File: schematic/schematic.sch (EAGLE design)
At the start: 4 parts

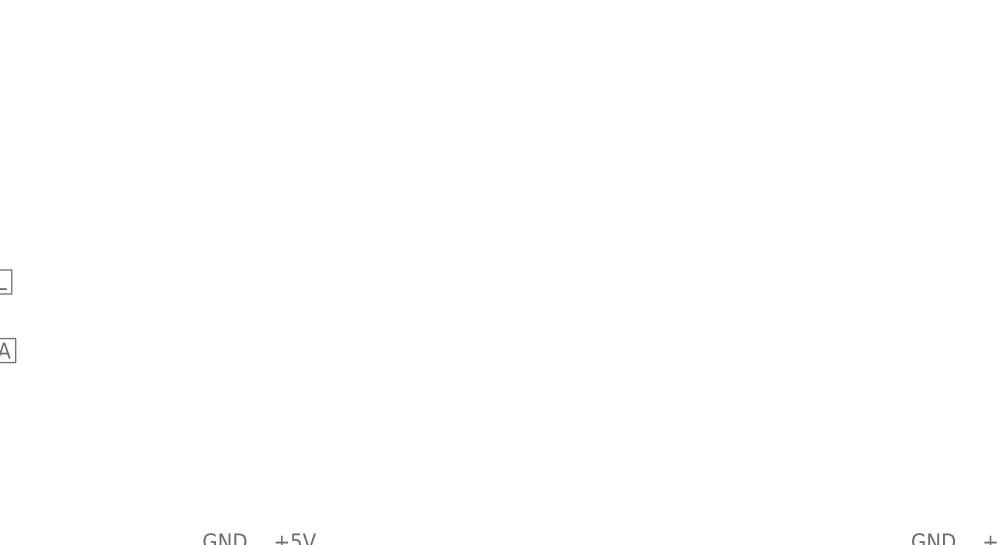
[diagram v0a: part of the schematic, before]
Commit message: Update schematic for radio module. Add eagle lib
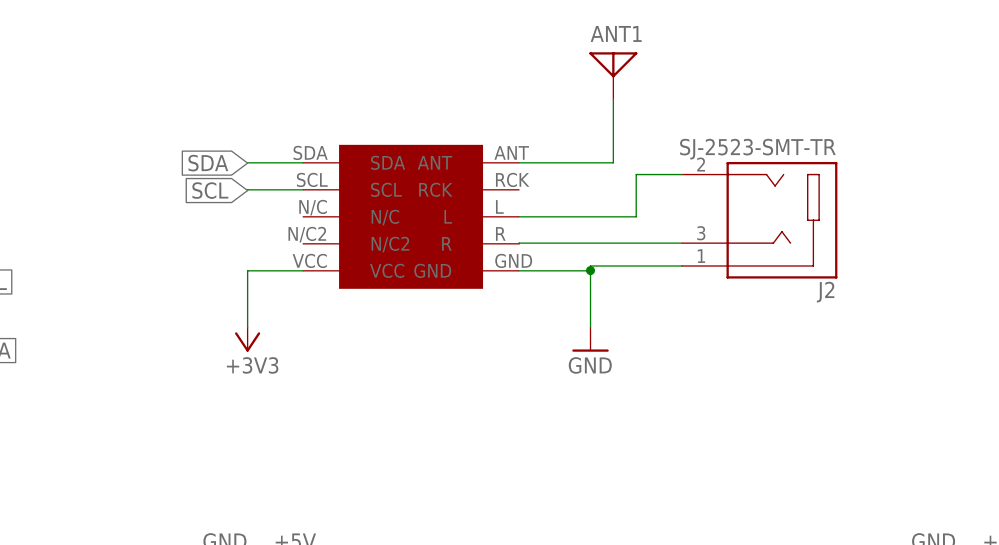
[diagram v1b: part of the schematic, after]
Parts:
- added ANT1: (no value), discrete:ANTENNA
- added J2: SJ-2523-SMT-TR, Audio Connectors:SJ-2523-SMT-TR
- added U$1: RDA, RDA:RDA
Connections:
- new net +3V3: U$1.VCC
- new net N$1: ANT1.1, U$1.ANT
- new net N$2: J2.TIP, U$1.L
- new net N$3: J2.RING, U$1.R
- net GND: now also J2.SLEEVE, U$1.GND
- net SCL: now also U$1.SCL
- net SDA: now also U$1.SDA
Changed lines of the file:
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@@
 <schematic_group name="USER_CONTROLLER"/>
 <schematic_group name="AUDIO_CONTOLLER"/>
+<schematic_group name="RADIO_MODULE"/>
 </groups>
 <parts>
@@
 <part name="R2" library="rcl" library_urn="urn:adsk.eagle:library:334" deviceset="R-EU_" device="0204/7" package3d_urn="urn:adsk.eagle:package:23498/2" value="4.7k"/>
 <part name="P+1" library="supply1" library_urn="urn:adsk.eagle:library:371" deviceset="+5V" device=""/>
+<part name="U$1" library="RDA" deviceset="RDA" device=""/>
+<part name="GND3" library="supply1" library_urn="urn:adsk.eagle:library:371" deviceset="GND" device=""/>
+<part name="ANT1" library="discrete" library_urn="urn:adsk.eagle:library:211" deviceset="ANTENNA" device="" package3d_urn="urn:adsk.eagle:package:12928/1"/>
+<part name="J2" library="Audio Connectors" library_urn="urn:adsk.eagle:library:16251796" deviceset="SJ-2523-SMT-TR" device="" package3d_urn="urn:adsk.eagle:package:16225688/4"/>
+<part name="+3V1" library="supply1" library_urn="urn:adsk.eagle:library:371" deviceset="+3V3" device=""/>
 </parts>
 <sheets>
@@
 <attribute name="VALUE" x="2.54" y="121.92" size="1.778" layer="96" rot="R180"/>
 </instance>
+<instance part="U$1" gate="G$1" x="63.5" y="124.46" smashed="yes" grouprefs="RADIO_MODULE"/>
+<instance part="GND3" gate="1" x="91.44" y="101.6" smashed="yes" grouprefs="RADIO_MODULE">
+<attribute name="VALUE" x="88.9" y="99.06" size="1.778" layer="96"/>
+</instance>
+<instance part="ANT1" gate="A" x="93.98" y="134.62" smashed="yes" grouprefs="RADIO_MODULE">
+<attribute name="NAME" x="91.44" y="135.89" size="1.778" layer="95"/>
+<attribute name="VALUE" x="96.52" y="129.54" size="1.778" layer="96"/>
+</instance>
+<instance part="J2" gate="G$1" x="114.3" y="116.078" smashed="yes" rot="R180" grouprefs="RADIO_MODULE">
+<attribute name="NAME" x="118.74991875" y="109.21475" size="1.77915" layer="95" rot="R180"/>
+<attribute name="VALUE" x="118.74648125" y="125.09688125" size="1.77835" layer="96" rot="R180"/>
+</instance>
+<instance part="+3V1" gate="G$1" x="53.34" y="101.6" smashed="yes" rot="R180">
+<attribute name="VALUE" x="50.8" y="99.06" size="1.778" layer="96"/>
+</instance>
 </instances>
 <busses>
@@
 <label x="20.32" y="109.22" size="1.778" layer="95" xref="yes" grouprefs="I2C"/>
 </segment>
+<segment>
+<pinref part="U$1" gate="G$1" pin="SCL"/>
+<wire x1="59.5" y1="119.46" x2="53.34" y2="119.46" width="0.1524" layer="91" grouprefs="RADIO_MODULE"/>
+<wire x1="53.34" y1="119.46" x2="53.34" y2="119.38" width="0.1524" layer="91" grouprefs="RADIO_MODULE"/>
+<label x="53.34" y="119.38" size="1.778" layer="95" rot="R180" xref="yes" grouprefs="RADIO_MODULE"/>
+</segment>
 </net>
 <net name="SDA" class="0">
@@
 <wire x1="15.24" y1="101.6" x2="20.32" y2="101.6" width="0.1524" layer="91" grouprefs="I2C"/>
 <label x="20.32" y="101.6" size="1.778" layer="95" xref="yes" grouprefs="I2C"/>
+</segment>
+<segment>
+<pinref part="U$1" gate="G$1" pin="SDA"/>
+<wire x1="59.5" y1="122.46" x2="53.34" y2="122.46" width="0.1524" layer="91" grouprefs="RADIO_MODULE"/>
+<label x="53.34" y="122.428" size="1.778" layer="95" rot="R180" xref="yes" grouprefs="RADIO_MODULE"/>
 </segment>
 </net>
@@
 <wire x1="129.54" y1="76.2" x2="129.54" y2="63.5" width="0.1524" layer="91" grouprefs="AUDIO_CONTOLLER"/>
 <wire x1="129.54" y1="63.5" x2="119.38" y2="63.5" width="0.1524" layer="91" grouprefs="AUDIO_CONTOLLER"/>
+</segment>
+<segment>
+<pinref part="U$1" gate="G$1" pin="GND"/>
+<pinref part="GND3" gate="1" pin="GND"/>
+<wire x1="83.5" y1="110.46" x2="91.44" y2="110.46" width="0.1524" layer="91" grouprefs="RADIO_MODULE"/>
+<pinref part="J2" gate="G$1" pin="SLEEVE"/>
+<wire x1="91.44" y1="110.46" x2="91.44" y2="104.14" width="0.1524" layer="91" grouprefs="RADIO_MODULE"/>
+<wire x1="101.6" y1="110.998" x2="91.44" y2="110.998" width="0.1524" layer="91" grouprefs="RADIO_MODULE"/>
+<wire x1="91.44" y1="110.998" x2="91.44" y2="110.49" width="0.1524" layer="91" grouprefs="RADIO_MODULE"/>
+<junction x="91.44" y="110.49" grouprefs="RADIO_MODULE"/>
+<wire x1="91.44" y1="110.49" x2="91.44" y2="110.46" width="0.1524" layer="91" grouprefs="RADIO_MODULE"/>
 </segment>
 </net>
@@
 </segment>
 </net>
+<net name="N$1" class="0">
+<segment>
+<pinref part="ANT1" gate="A" pin="1"/>
+<wire x1="93.98" y1="129.54" x2="93.98" y2="122.46" width="0.1524" layer="91" grouprefs="RADIO_MODULE"/>
+<pinref part="U$1" gate="G$1" pin="ANT"/>
+<wire x1="93.98" y1="122.46" x2="83.5" y2="122.46" width="0.1524" layer="91" grouprefs="RADIO_MODULE"/>
+</segment>
+</net>
+<net name="N$2" class="0">
+<segment>
+<pinref part="J2" gate="G$1" pin="TIP"/>
+<pinref part="U$1" gate="G$1" pin="L"/>
+<wire x1="101.6" y1="121.158" x2="96.52" y2="121.158" width="0.1524" layer="91" grouprefs="RADIO_MODULE"/>
+<wire x1="96.52" y1="121.158" x2="96.52" y2="116.46" width="0.1524" layer="91" grouprefs="RADIO_MODULE"/>
+<wire x1="96.52" y1="116.46" x2="83.5" y2="116.46" width="0.1524" layer="91" grouprefs="RADIO_MODULE"/>
+</segment>
+</net>
+<net name="N$3" class="0">
+<segment>
+<pinref part="J2" gate="G$1" pin="RING"/>
+<pinref part="U$1" gate="G$1" pin="R"/>
+<wire x1="101.6" y1="113.538" x2="83.5" y2="113.538" width="0.1524" layer="91" grouprefs="RADIO_MODULE"/>
+<wire x1="83.5" y1="113.538" x2="83.5" y2="113.46" width="0.1524" layer="91" grouprefs="RADIO_MODULE"/>
+</segment>
+</net>
+<net name="+3V3" class="0">
+<segment>
+<wire x1="53.34" y1="104.14" x2="53.34" y2="110.46" width="0.1524" layer="91" grouprefs="RADIO_MODULE"/>
+<pinref part="U$1" gate="G$1" pin="VCC"/>
+<wire x1="53.34" y1="110.46" x2="59.5" y2="110.46" width="0.1524" layer="91" grouprefs="RADIO_MODULE"/>
+<pinref part="+3V1" gate="G$1" pin="+3V3"/>
+</segment>
+</net>

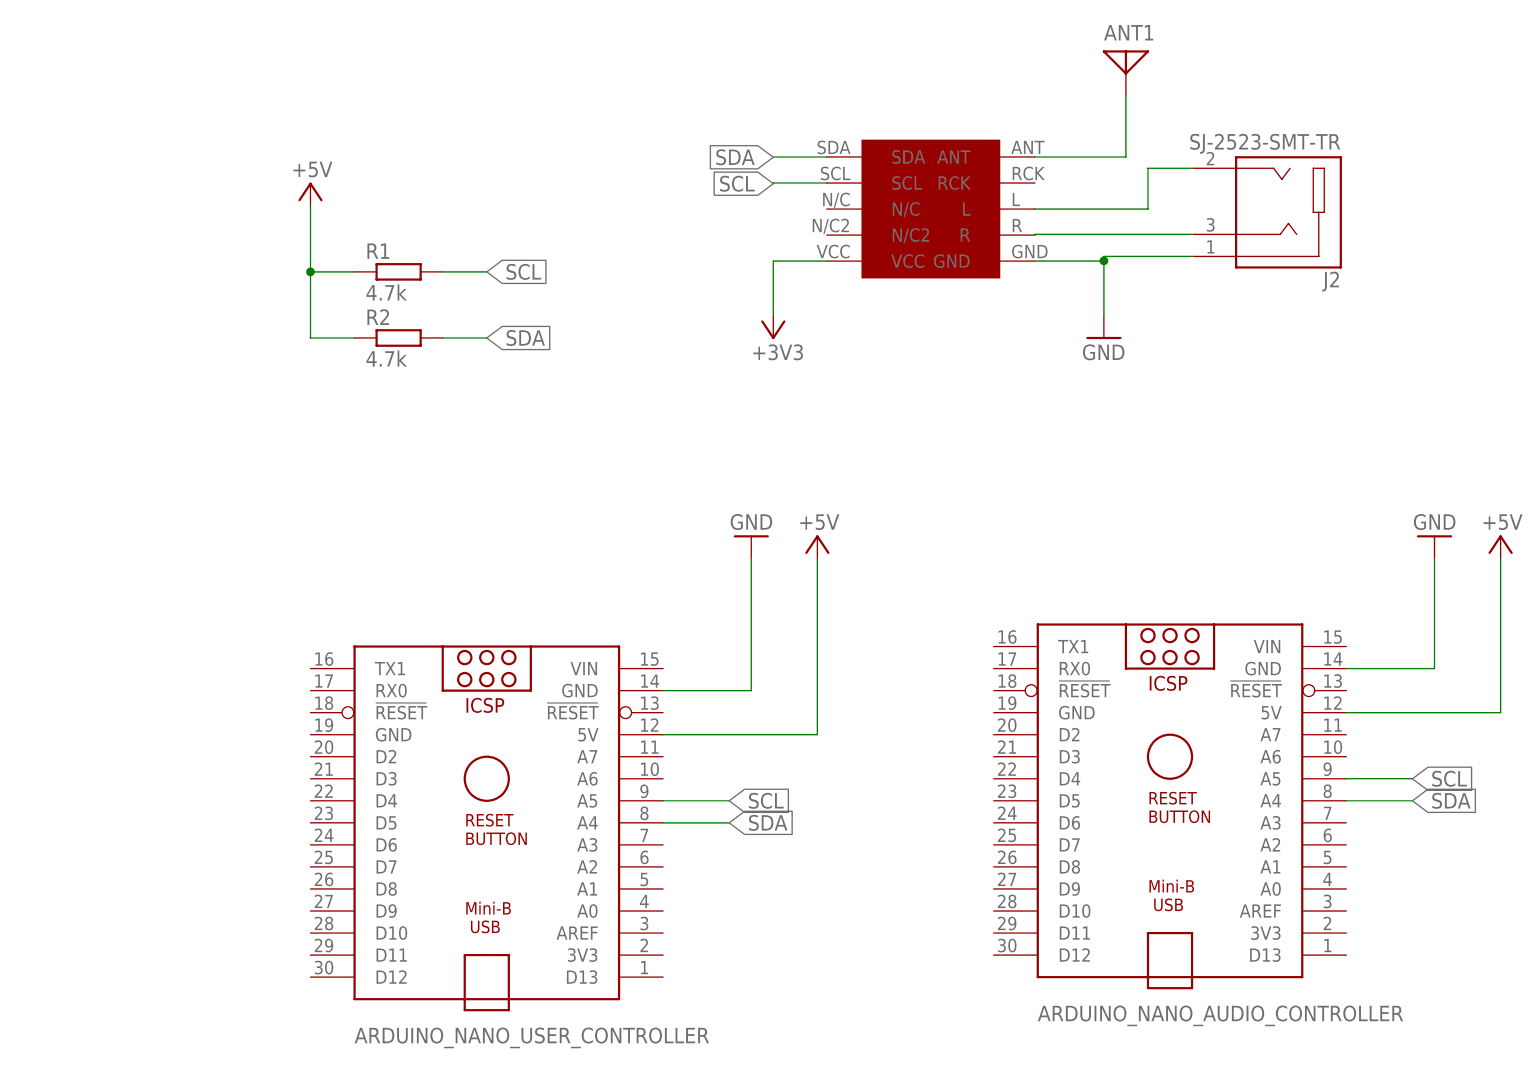
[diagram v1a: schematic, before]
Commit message: Add freq potentiometer to schematic
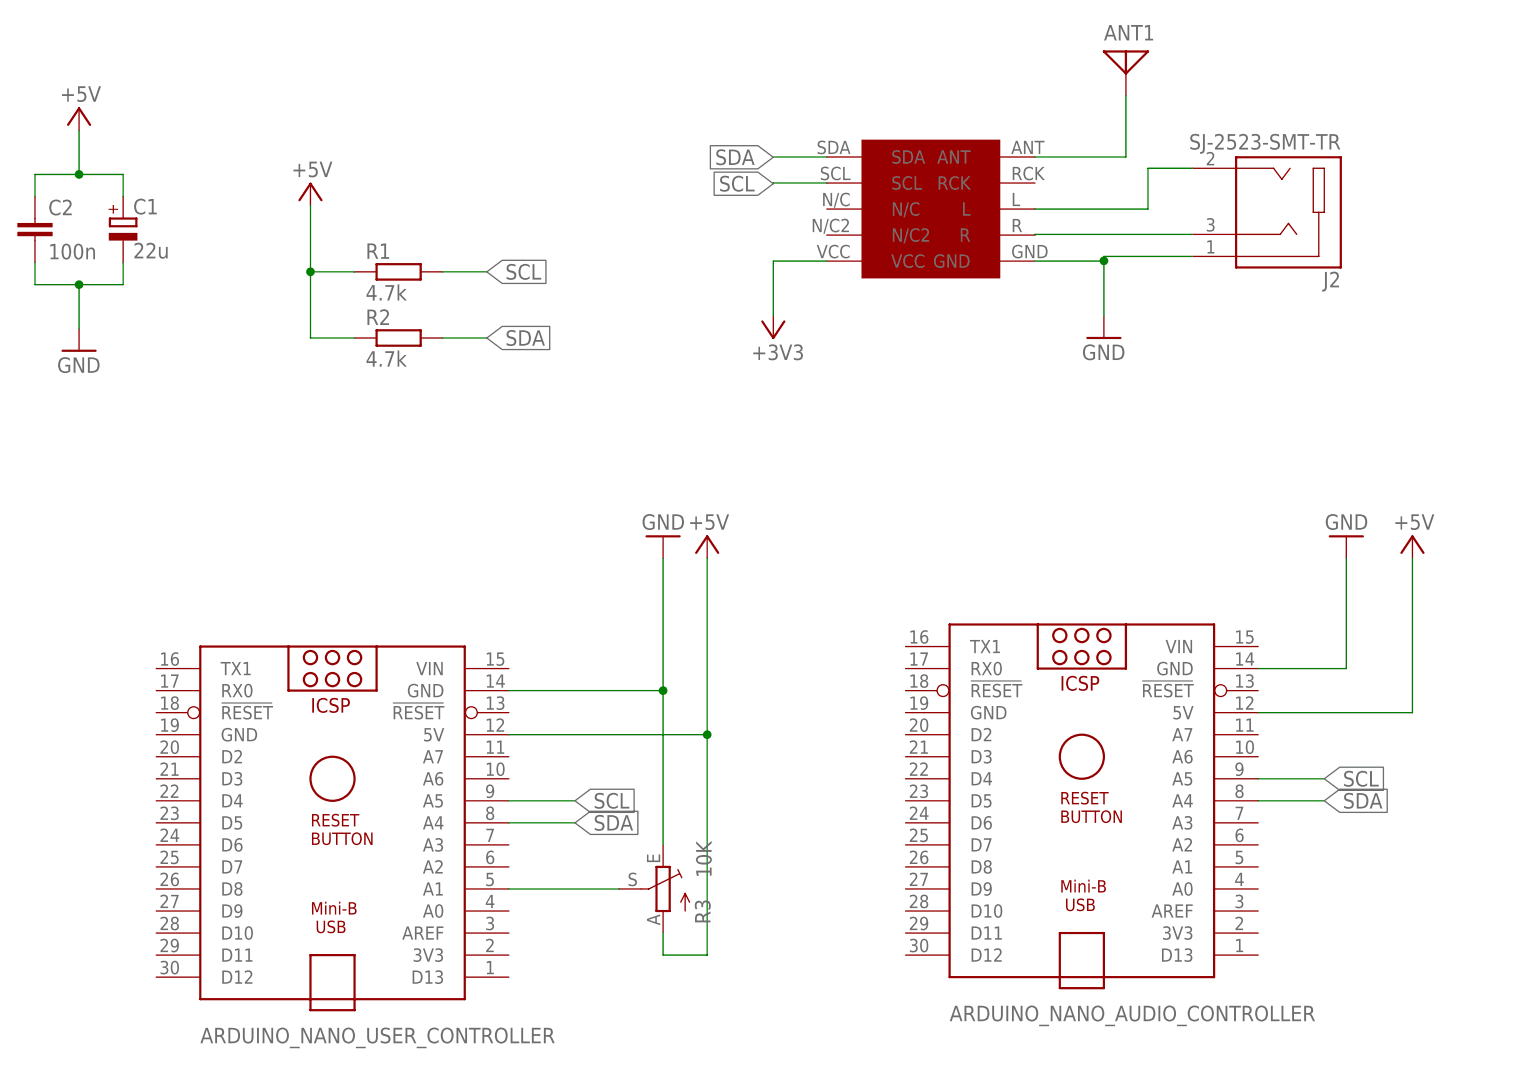
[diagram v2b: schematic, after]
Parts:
- added C1: 22u, rcl:CPOL-EUE2,5-6E
- added C2: 100n, rcl:C-EU025-024X044
- added R3: 10K, pot:TRIM_EU-B25V
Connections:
- new net N$4: ARDUINO_NANO_USER_CONTROLLER.A0, ARDUINO_NANO_USER_CONTROLLER.A1, R3.S
- net +5V: now also C1.+, C2.1, R3.A
- net GND: now also C1.-, C2.2, R3.E
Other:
- moved on the sheet: ARDUINO_NANO_AUDIO_CONTROLLER, ARDUINO_NANO_USER_CONTROLLER
